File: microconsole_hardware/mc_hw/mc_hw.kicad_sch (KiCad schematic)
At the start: 39 parts, among them SW1 DPAD - UP, SW10 START, SW11 L1, SW12 R1, SW13 L2, SW14 R2, SW16 Joystick, SW17 Joystick, SW2 DPAD - DOWN, SW3 DPAD - LEFT, SW4 DPAD - RIGHT, SW5 A, SW6 B, SW7 X, SW8 Y, SW9 SELECT, U1 ILI9341 / ST7796S SPI LCD, U2 MAX98357A, U3 MCP23017x-x-SO

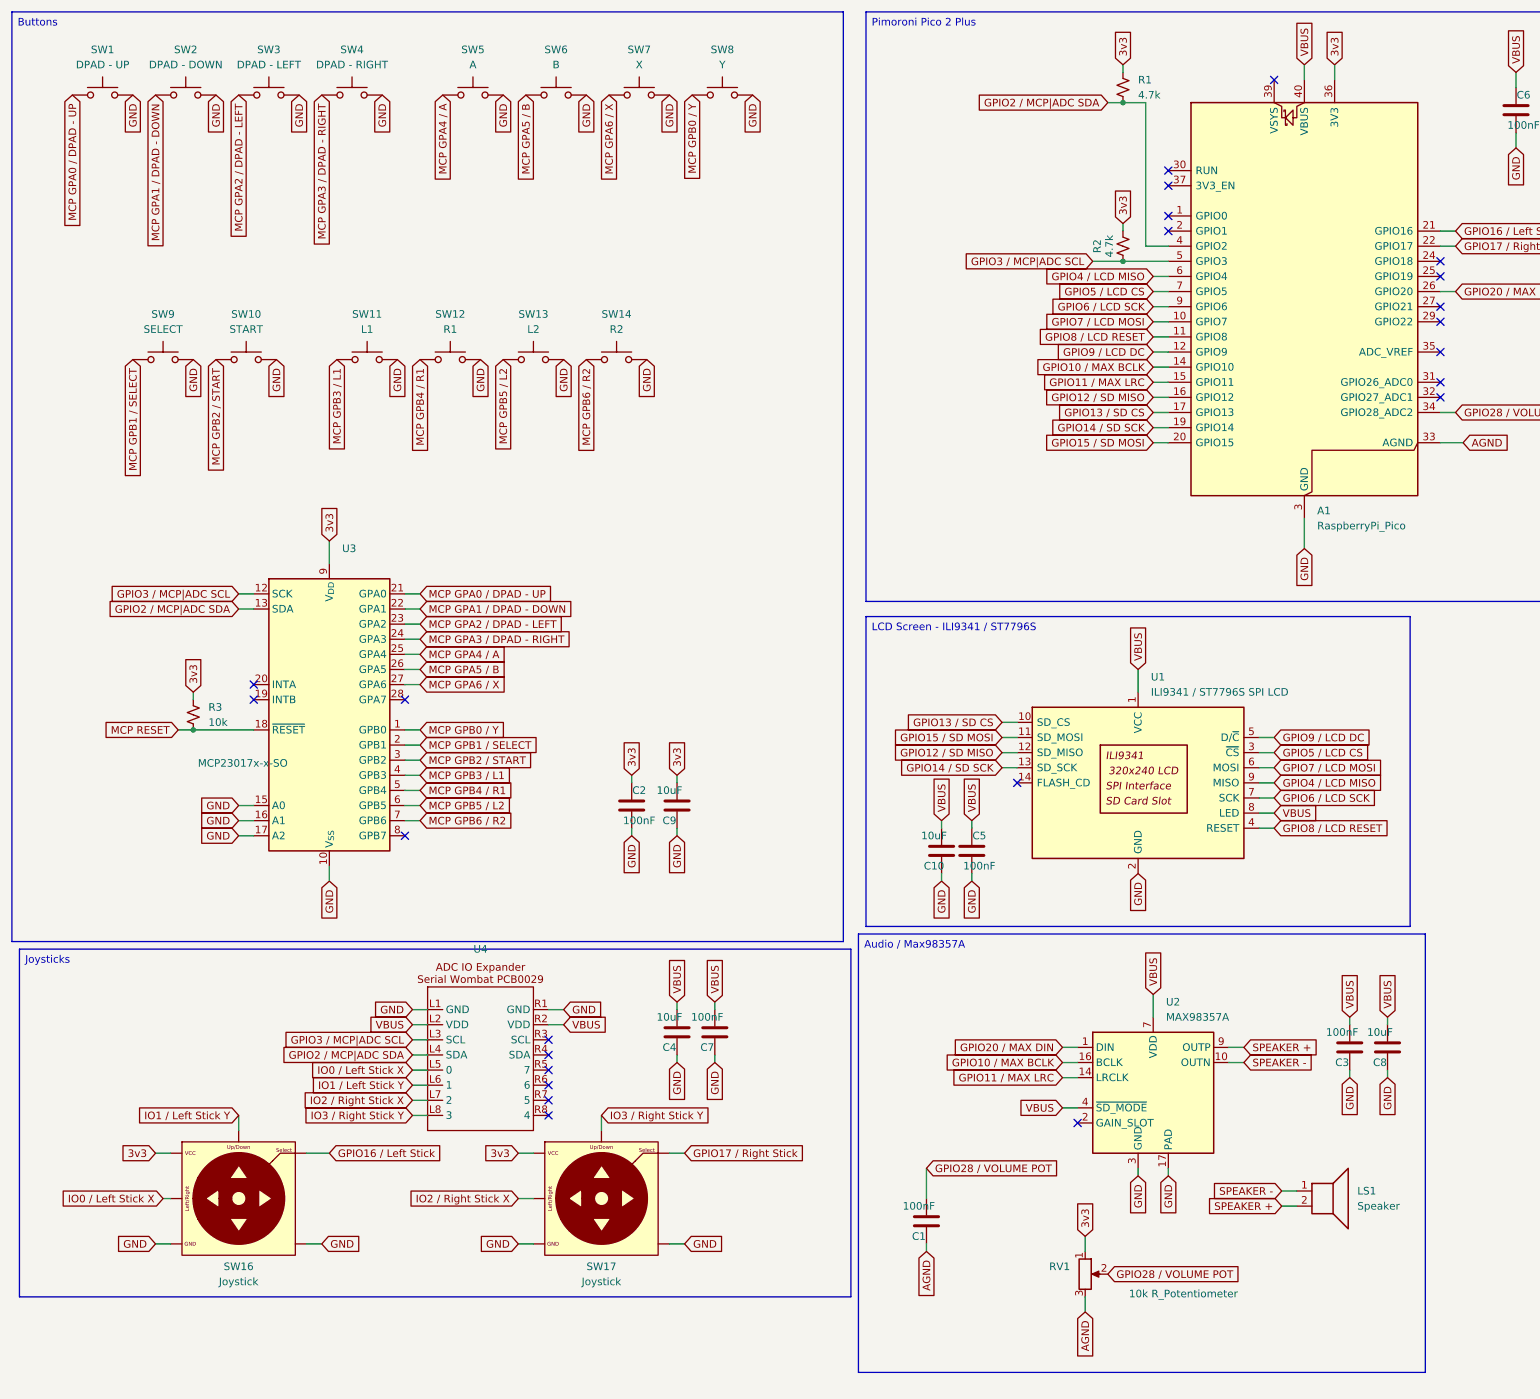
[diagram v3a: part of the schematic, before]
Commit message: Fix TFT library/symbol pin mapping
Updated the TFT symbol and PCB metadata to match the actual LCD pin names and net mapping, corrected the footprint library alias, and removed the stale DRC report generated from the outdated symbol/footprint state.
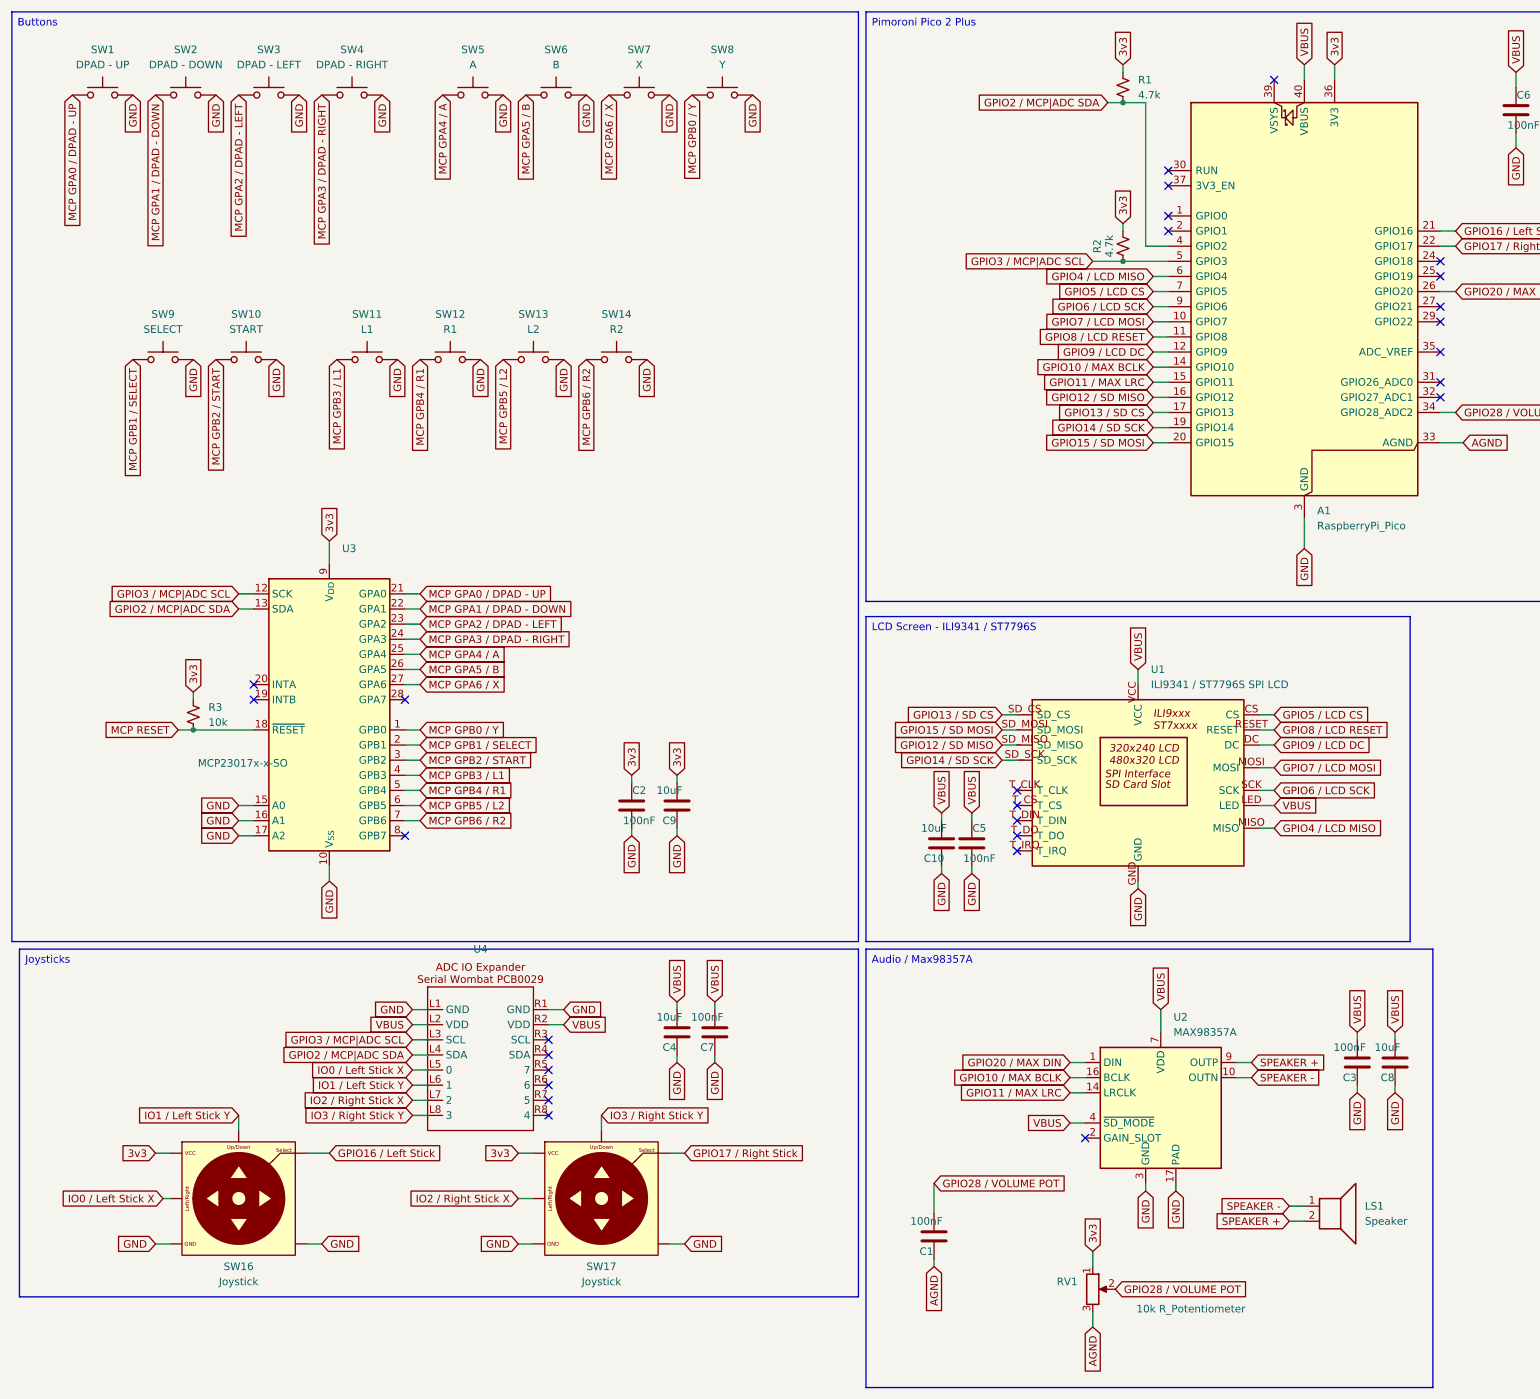
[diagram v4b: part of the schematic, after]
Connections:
- net GND: now also U1.GND; no longer U1.2 (GND)
- net GPIO12 / SD MISO: now also U1.SD_MISO; no longer U1.12 (SD_MISO)
- net GPIO13 / SD CS: now also U1.SD_CS; no longer U1.10 (SD_CS)
- net GPIO14 / SD SCK: now also U1.SD_SCK; no longer U1.13 (SD_SCK)
- net GPIO15 / SD MOSI: now also U1.SD_MOSI; no longer U1.11 (SD_MOSI)
- net GPIO4 / LCD MISO: now also U1.MISO; no longer U1.9 (MISO)
- net GPIO5 / LCD CS: now also U1.CS; no longer U1.3 (~{CS})
- net GPIO6 / LCD SCK: now also U1.SCK; no longer U1.7 (SCK)
- net GPIO7 / LCD MOSI: now also U1.MOSI; no longer U1.6 (MOSI)
- net GPIO8 / LCD RESET: now also U1.RESET; no longer U1.4 (RESET)
- net GPIO9 / LCD DC: now also U1.DC; no longer U1.5 (D/~{C})
- net VBUS: now also U1.LED, U1.VCC; no longer U1.1 (VCC), U1.8 (LED)
- no-connect marks 24 -> 28
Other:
- moved on the sheet: C1, C10, C3, C5, C8, LS1, RV1, U2

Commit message: hardware update
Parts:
- added C14, C15: 10uF, symbol Device:C
- added D1: LED - GREEN, PCM_SparkFun-Resistor:R_0603_1608Metric, symbol Device:LED
- added D2: LED - ORANGE, PCM_SparkFun-Resistor:R_0603_1608Metric, symbol Device:LED
- added D3: LED - RED, PCM_SparkFun-Resistor:R_0603_1608Metric, symbol Device:LED
- added J1: USB_C_Receptacle_USB2.0_16P, symbol Connector:USB_C_Receptacle_USB2.0_16P
- added J2: JST_1mm_4 - BAT IN, PCM_SparkFun-Connector:JST_1x04_P1.0mm_Horizontal_SMD, symbol PCM_SparkFun-Connector:Conn_01x04_JST_P1.0mm_Horizontal_SMD
- added J3: JST_1mm_4 - LOAD, PCM_SparkFun-Connector:JST_1x04_P1.0mm_Horizontal_SMD, symbol PCM_SparkFun-Connector:Conn_01x04_JST_P1.0mm_Horizontal_SMD
- added JP1, JP2: (no value), PCM_SparkFun-Jumper:Jumper_2_NO, symbol PCM_SparkFun-Jumper:SolderJumper_2_Open
- added R10: 150k, PCM_SparkFun-Resistor:R_0603_1608Metric, symbol PCM_SparkFun-Resistor:0.47_0603
- added R4, R5, R6, R8: 1k, PCM_SparkFun-Resistor:R_0603_1608Metric, symbol PCM_SparkFun-Resistor:0.47_0603
- added R7: 2k, PCM_SparkFun-Resistor:R_0603_1608Metric, symbol PCM_SparkFun-Resistor:0.47_0603
- added R9: 10k, PCM_SparkFun-Resistor:R_0603_1608Metric, symbol PCM_SparkFun-Resistor:0.47_0603
- added U5: MCP73833_MSOP, PCM_SparkFun-Semiconductor-Standard:MSOP-10_3x3mm_P0.5mm, symbol PCM_SparkFun-IC-Power:MCP73833
- SW16, SW17: footprint PCM_SparkFun-Switch:Joystick_PTH -> microconsole:Joystick_PTH
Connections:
- net GND: now also C14.1, C15.1, J1.A1 (GND), J1.A12 (GND), J1.B1 (GND), J1.B12 (GND), J1.SH (SHIELD), J2.4, J3.4, JP1.2 (B), R10.2, R7.2, R9.2, U5.5 (VSS)
- net VBUS renamed VDD
- net VDD: now also C14.2, C15.2, D1.2 (A), D2.2 (A), D3.2 (A), J1.A4 (VBUS), J1.A9 (VBUS), J1.B4 (VBUS), J1.B9 (VBUS), J2.1, J3.1, JP1.1 (A), U5.1 (VDD), U5.10 (V_{BAT}), U5.2 (VDD), U5.9 (V_{BAT})
- new net: R10.1, R8.1, R9.1
- new net: R8.2, U5.8 (THERM)
- new net: D1.1 (K), R4.2
- new net: D3.1 (K), R6.2
- new net: JP2.1 (A), R4.1, U5.4 (STAT2)
- new net: JP2.2 (B), R5.1, U5.3 (STAT1)
- new net: R6.1, U5.7 (~{PG})
- new net: D2.1 (K), R5.2
- new net: R7.1, U5.6 (PROG)
- no-connect marks 28 -> 40

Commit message: hardware update
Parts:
- removed C10, C11, C13, C9: 10uF, symbol Device:C
- removed C12, C2, C5, C6: 100nF, symbol Device:C
- removed R3: 10k, PCM_SparkFun-Resistor:R_0603_1608Metric, symbol PCM_SparkFun-Resistor:0.47_0603
- removed SW16, SW17: Joystick, microconsole:Joystick_PTH, symbol PCM_SparkFun-Switch:Joystick_PTH
- removed U1: ILI9341 / ST7796S SPI LCD, microconsole_hardware:TFT, symbol microconsole:ili9xxx/st7xxxx
- removed U3: MCP23017x-x-SO, Package_SO:SOIC-28W_7.5x17.9mm_P1.27mm, symbol Interface_Expansion:MCP23017x-x-SO
- added C18, C20, C22, C24, C27: 100nF 50V X7R, project_parts:C_0805_2012Metric_KEMET_IPC-B, symbol project_parts:C0805C104K5RAC7210
- added C19, C21, C23, C25, C26: 1206ZD106KAT2A, project_parts:C1206, symbol project_parts:1206ZD106KAT2A
- added DS2: MSP4021, project_parts:LCD_MSP4021_4.0in_SPI_ST7796_1x14_P2.54mm, symbol project_parts:MSP4021
- added LS4, LS6: 8R 1W, Connector_Molex:Molex_PicoBlade_53047-0210_1x02_P1.25mm_Vertical, symbol project_parts:AS02008MR-2-LWC30
- added LS5: 8R 3W, project_parts:Speaker_WirePads_1x02_P3.50mm_D1.0mm, symbol project_parts:AS03208AS-HT
- added R11: 10k, PCM_SparkFun-Resistor:R_0603_1608Metric, symbol PCM_SparkFun-Resistor:0.47_0603
- added R13: RC0805FR-0710KL, project_parts:R0805, symbol project_parts:RC0805FR-0710KL
- added R14: RC0805FR-074K7L, project_parts:R0805, symbol project_parts:RC0805FR-074K7L
- added RV3: 10k Lin, project_parts:PTV09A2015FB103, symbol project_parts:PTV09A-2015F-B103
- added SW15, SW16: Joystick, project_parts:GINFULL HallEffect Joystick PTH, symbol project_parts:GINFULL_HallEffect_Joystick_PTH
- added SW18: TL3301NF160QG, project_parts:KEY-SMD_4P-L6.0-W6.0-P4.50-LS10.0, symbol project_parts:TL3301NF160QG
- added U12: S2B-PH-K-S, project_parts:CONN-TH_S2B-PH-K-S-LF-SN, symbol project_parts:S2B-PH-K-S
- added U13: MCP23017-E/SO, project_parts:SOIC-28_L18.0-W7.5-P1.27-LS10.3-BL, symbol project_parts:MCP23017-E_SO
- added U14: ADS7828E/2K5, project_parts:TSSOP-16_L5.0-W4.4-P0.65-LS6.4-BL, symbol project_parts:ADS7828E_2K5
- added U15: PAM8302AADCR, project_parts:SOP-8_L4.9-W3.9-P1.27-LS6.0-BL, symbol project_parts:PAM8302AADCR
- added U16: PAM8406DR, project_parts:SOIC-16_L9.9-W3.9-P1.27-LS6.0-BL, symbol project_parts:PAM8406DR
- added U17: PCM5102APWR, project_parts:TSSOP-20_L6.5-W4.4-P0.65-LS6.4-BL, symbol project_parts:PCM5102APWR
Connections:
- net 3v3: now also C22.1, C23.2, C24.1, C25.1, R11.2, SW15.VCC, SW16.VCC, U13.9 (VDD)
- net GND: now also C20.2, C21.1, C22.2, C23.1, C24.2, C25.2, C26.1, C27.1, DS2.2 (GND), SW15.GND, SW16.GND, U13.10 (VSS), U13.15 (A0), U13.16 (A1), U13.17 (A2)
- net GPIO12 / SD MISO: now also DS2.17 (SD_MISO)
- net GPIO13 / SD CS: now also DS2.15 (SD_CS)
- net GPIO14 / SD SCK: now also DS2.18 (SD_SCK)
- net GPIO15 / SD MOSI: now also DS2.16 (SD_MOSI)
- net GPIO16 / Left Stick: now also SW15.Select
- net GPIO17 / Right Stick: now also SW16.Select
- net GPIO2 / MCP|ADC SDA: now also U13.13 (SDA)
- net GPIO3 / MCP|ADC SCL: now also U13.12 (SCL)
- net GPIO4 / LCD MISO: now also DS2.9 (SDO(MISO))
- net GPIO5 / LCD CS: now also DS2.3 (CS)
- net GPIO6 / LCD SCK: now also DS2.7 (SCK)
- net GPIO7 / LCD MOSI: now also DS2.6 (SDI(MOSI))
- net GPIO8 / LCD RESET: now also DS2.4 (RESET)
- net GPIO9 / LCD DC: now also DS2.5 (DC/RS)
- net IO0 / Left Stick X: now also SW15.Horizontal
- net IO1 / Left Stick Y: now also SW15.Vertical
- net IO2 / Right Stick X: now also SW16.Horizontal
- net IO3 / Right Stick Y: now also SW16.Vertical
- net MCP GPA0 / DPAD - UP: now also U13.21 (GPA0)
- net MCP GPA1 / DPAD - DOWN: now also U13.22 (GPA1)
- net MCP GPA2 / DPAD - LEFT: now also U13.23 (GPA2)
- net MCP GPA3 / DPAD - RIGHT: now also U13.24 (GPA3)
- net MCP GPA4 / A: now also U13.25 (GPA4)
- net MCP GPA5 / B: now also U13.26 (GPA5)
- net MCP GPA6 / X: now also U13.27 (GPA6)
- net MCP GPB0 / Y: now also U13.1 (GPB0)
- net MCP GPB1 / SELECT: now also U13.2 (GPB1)
- net MCP GPB2 / START: now also U13.3 (GPB2)
- net MCP GPB3 / L1: now also U13.4 (GPB3)
- net MCP GPB4 / R1: now also U13.5 (GPB4)
- net MCP GPB5 / L2: now also U13.6 (GPB5)
- net MCP GPB6 / R2: now also U13.7 (GPB6)
- net MCP RESET: now also R11.1, U13.18 (~{RESET})
- net VDD: now also C20.1, C21.2, C26.2, C27.2, DS2.1 (VCC), DS2.8 (LED)
- no-connect marks 40 -> 42
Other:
- note added: "NEED TO SWAP BUTTONS"
- moved on the sheet: A1, C1, C3, C8, LS1, R1, R2, RV1, SW1, SW10, SW11, SW12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

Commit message: update
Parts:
- removed C1, C3: 100nF, symbol Device:C
- removed C8: 10uF, symbol Device:C
- removed LS1: Speaker, symbol Device:Speaker
- removed RV1: 10k R_Potentiometer, symbol Device:R_Potentiometer
- removed U2: MAX98357A, Package_DFN_QFN:TQFN-16-1EP_3x3mm_P0.5mm_EP1.23x1.23mm, symbol microconsole:MAX98357A
- added C10, C2, C5, C6, C9: 2.2uF, PCM_SparkFun-Capacitor:C_0805_2012Metric, symbol PCM_SparkFun-Capacitor:2.2uF_0805_25V_20%
- added C11, C12: 0.47uF, PCM_SparkFun-Capacitor:C_0805_2012Metric, symbol PCM_SparkFun-Capacitor:2.2uF_0805_25V_20%
- added C13, C16, C17: 1uF, PCM_SparkFun-Capacitor:C_0805_2012Metric, symbol PCM_SparkFun-Capacitor:2.2uF_0805_25V_20%
- added C28, C29, C31, C33, C37: 100nF 50V X7R, project_parts:C_0805_2012Metric_KEMET_IPC-B, symbol project_parts:C0805C104K5RAC7210
- added C30, C32, C34: 1206ZD106KAT2A, project_parts:C1206, symbol project_parts:1206ZD106KAT2A
- added C35: 33nF, PCM_SparkFun-Capacitor:C_0805_2012Metric, symbol PCM_SparkFun-Capacitor:2.2uF_0805_25V_20%
- added C36, C38: 0.22uF, PCM_SparkFun-Capacitor:C_0805_2012Metric, symbol PCM_SparkFun-Capacitor:2.2uF_0805_25V_20%
- added R12, R15, R19, R22, R23, R26: 10k OHM, PCM_SparkFun-Resistor:R_0603_1608Metric, symbol PCM_SparkFun-Resistor:R
- added R16, R3: 470 OHM, PCM_SparkFun-Resistor:R_0603_1608Metric, symbol PCM_SparkFun-Resistor:R
- added R17, R18, R20, R21: 22k OHM, PCM_SparkFun-Resistor:R_0603_1608Metric, symbol PCM_SparkFun-Resistor:R
- added R24: 33k OHM, PCM_SparkFun-Resistor:R_0603_1608Metric, symbol PCM_SparkFun-Resistor:R
- added R25: 4.7k OHM, PCM_SparkFun-Resistor:R_0603_1608Metric, symbol PCM_SparkFun-Resistor:R
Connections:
- net 3v3: now also RV3.3 (CW), R26.1
- net GND: now also RV3.1 (CCW), U15.7 (GND), U16.11 (GND), U16.15 (PGNDR), U16.2 (PGNDL), U17.10 (DEMP), U17.11 (FLT), U17.12 (SCK), U17.16 (FMT), U17.19 (DGND), U17.3 (CPGND), U17.9 (AGND), C10.2, C13.2, C16.1, C17.1, C28.1, C29.1, C30.1, C30.2, C31.1, C32.1, C32.2, C33.1, C34.1, C34.2, C35.2, C37.1, C38.2, C5.2, C9.2, R20.2, R21.2, R25.2, R26.2
- net GPIO10 / MAX BCLK: now also U17.13 (BCK)
- net GPIO11 / MAX LRC: now also U17.15 (LRCK)
- net GPIO20 / MAX DIN: now also U17.14 (DIN)
- net VOL_ADC: now reaches RV3.2 (WIPER)
- net VOL_ADC: now also C37.2
- net 3v3_AUDIO: now reaches U17.1 (CPVDD)
- net 3v3_AUDIO: now also U17.20 (DVDD), U17.8 (AVDD), C29.2, C31.2, C33.2, R15.1
- net at U17.17 (XSMT): now also R15.2
- net at U17.18 (LDOO): now also C28.2
- net at U17.2 (CAPP): now also C2.1
- net at U17.4 (CAPM): now also C2.2
- net at U17.5 (VNEG): now also C5.1
- net at U17.6 (OUTL): now also R3.1
- net at U17.7 (OUTR): now also R16.1
- net at U16.1 (+OUT_L): now also LS6.2 (-_(black))
- net at U16.10 (INR): now also C11.1
- net at U16.12 (~{SHDN}): now also R19.2
- net AMP_VDD: now reaches U16.13 (PVDDR)
- net AMP_VDD: now also U15.6 (VDD), U16.4 (PVDDL), U16.6 (VDD), U16.9 (MODE), C16.2, C17.2, R12.2, R19.1
- net at U16.14 (-OUT_R): now also LS4.2 (-_(black))
- net at U16.16 (+OUT_R): now also LS4.1 (+_(red))
- net at U16.3 (-OUT_L): now also LS6.1 (+_(red))
- net at U16.5 (~{MUTE}): now also R12.1
- net at U16.7 (INL): now also C12.1
- net at U16.8 (VREF): now also C13.1
- net at LS5.1 (+): now also U15.8 (VO-)
- net at LS5.2 (-): now also U15.5 (VO+)
- net at U15.3 (IN+): now also C36.2
- net at U15.4 (IN-): now also C38.1
- new net: C11.2, R18.1, R20.1
- new net: C12.2, R17.1, R21.1
- new net CENTER_FEED: C35.1, C36.1, R24.1, R25.1
- new net CENTER_MIX: R22.1, R23.2, R24.2
- new net DAC_L: C9.1, R17.2, R22.2, R3.2
- new net DAC_R: C10.1, R16.2, R18.2, R23.1
- no-connect marks 42 -> 44
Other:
- moved on the sheet: LS4, LS5, LS6, RV3, U15, U16

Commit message: update
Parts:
- removed C6: 2.2uF, PCM_SparkFun-Capacitor:C_0805_2012Metric, symbol PCM_SparkFun-Capacitor:2.2uF_0805_25V_20%
- added C39, C40: 1206ZD106KAT2A, project_parts:C1206, symbol project_parts:1206ZD106KAT2A
- added C41: 100nF 50V X7R, project_parts:C_0805_2012Metric_KEMET_IPC-B, symbol project_parts:C0805C104K5RAC7210
- added C42: 1uF, PCM_SparkFun-Capacitor:C_0805_2012Metric, symbol PCM_SparkFun-Capacitor:2.2uF_0805_25V_20%
- added C43: 10uF, PCM_SparkFun-Capacitor:C_0805_2012Metric, symbol PCM_SparkFun-Capacitor:2.2uF_0805_25V_20%
- C10, C9: value 2.2uF -> 2.2nF
- R26: value 10k OHM -> 100k OHM
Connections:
- net 3v3: no longer R26.1
- net AMP_VDD: now also R26.1, C39.2, C40.1, C42.1, C43.1
- net GND: now also C39.1, C40.2, C41.1, C42.2, C43.2; no longer R26.2
- net VOL_ADC: now also U14.6 (CH5)
- net at U16.1 (+OUT_L): now also LS6.1 (+_(red)); no longer LS6.2 (-_(black))
- net at U16.3 (-OUT_L): now also LS6.2 (-_(black)); no longer LS6.1 (+_(red))
- net at U15.1 (~{SD}): now also R26.2, C41.2
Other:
- moved on the sheet: C10, C11, C12, C13, C16, C17, C2, C28, C29, C30, C31, C32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
